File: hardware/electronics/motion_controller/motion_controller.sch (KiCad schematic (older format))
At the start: 181 parts, among them K1 CONN_3, K10 CONN_3, K11 CONN_3, K12 CONN_3, K13 CONN_3, K14 CONN_3, K15 CONN_3, K2 CONN_3, K3 CONN_3, K4 CONN_3, K5 CONN_3, K6 CONN_3, K7 CONN_3, K8 CONN_3, K9 CONN_3, P1 CONN_2, P10 CONN_4, P11 CONN_4, P12 CONN_4, P13 CONN_2, P14 CONN_2, P15 CONN_2, P16 CONN_2, P17 CONN_2, P18 CONN_2, P19 CONN_2X2, P2 CONN_5X2, P20 CONN_2X2, P21 CONN_2, P22 CONN_2, P23 CONN_2, P24 CONN_2, P25 CONN_2, P26 CONN_2X2, P27 CONN_2, P28 CONN_2, P29 CONN_2, P3 CONN_2X2, P4 CONN_2, P5 CONN_34X2, P6 CONN_4, P7 CONN_4, P8 CONN_4, P9 CONN_4, U1 TEENSY3.1, U10 OP07, U12 OP07, U14 OP07, U16 OP07, U18 OP07, U2 NC7WZ04, U20 OP07, U22 OP07, U24 OP07, U26 OP07, U27 MEA1D0512SC, U3 NC7WZ16, U4 NC7WZ16, U5 SSR_DC_6PIN, U6 MAX6176AASA+, U8 OP07

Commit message: Worked on layout.
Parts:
- renumbered U14 to U10, U16 to U11, U18 to U12, U20 to U13, U22 to U14, U24 to U15, U26 to U16, U27 to U17, U8 to U7, U10 to U8, U12 to U9
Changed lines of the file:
@@
 Stepper/Servo Motors
 $Comp
-L OP07 U8
+L OP07 U7
 U 1 1 56F328BD
 P 13850 1450
-F 0 "U8" H 13850 1800 60  0000 C CNN
+F 0 "U7" H 13850 1800 60  0000 C CNN
 F 1 "OP07" H 13850 1150 60  0000 C CNN
 F 2 "~" H 13880 1450 60  0000 C CNN
@@
 GND
 $Comp
-L OP07 U10
+L OP07 U8
 U 1 1 56F34AA5
 P 13850 2550
-F 0 "U10" H 13850 2900 60  0000 C CNN
+F 0 "U8" H 13850 2900 60  0000 C CNN
 F 1 "OP07" H 13850 2250 60  0000 C CNN
 F 2 "~" H 13880 2550 60  0000 C CNN
@@
 10V_REF
 $Comp
-L OP07 U12
+L OP07 U9
 U 1 1 56F34AE7
 P 13850 3650
-F 0 "U12" H 13850 4000 60  0000 C CNN
+F 0 "U9" H 13850 4000 60  0000 C CNN
 F 1 "OP07" H 13850 3350 60  0000 C CNN
 F 2 "~" H 13880 3650 60  0000 C CNN
@@
 10V_REF
 $Comp
-L OP07 U14
+L OP07 U10
 U 1 1 56F34B29
 P 13850 4750
-F 0 "U14" H 13850 5100 60  0000 C CNN
+F 0 "U10" H 13850 5100 60  0000 C CNN
 F 1 "OP07" H 13850 4450 60  0000 C CNN
 F 2 "~" H 13880 4750 60  0000 C CNN
@@
 10V_REF
 $Comp
-L OP07 U16
+L OP07 U11
 U 1 1 56F34B6B
 P 13850 5800
-F 0 "U16" H 13850 6150 60  0000 C CNN
+F 0 "U11" H 13850 6150 60  0000 C CNN
 F 1 "OP07" H 13850 5500 60  0000 C CNN
 F 2 "~" H 13880 5800 60  0000 C CNN
@@
 10V_REF
 $Comp
-L OP07 U18
+L OP07 U12
 U 1 1 56F34BAD
 P 13850 6900
-F 0 "U18" H 13850 7250 60  0000 C CNN
+F 0 "U12" H 13850 7250 60  0000 C CNN
 F 1 "OP07" H 13850 6600 60  0000 C CNN
 F 2 "~" H 13880 6900 60  0000 C CNN
@@
 10V_REF
 $Comp
-L OP07 U20
+L OP07 U13
 U 1 1 56F34BEF
 P 13850 8000
-F 0 "U20" H 13850 8350 60  0000 C CNN
+F 0 "U13" H 13850 8350 60  0000 C CNN
 F 1 "OP07" H 13850 7700 60  0000 C CNN
 F 2 "~" H 13880 8000 60  0000 C CNN
@@
 10V_REF
 $Comp
-L OP07 U22
+L OP07 U14
 U 1 1 56F34C31
 P 13850 9100
-F 0 "U22" H 13850 9450 60  0000 C CNN
+F 0 "U14" H 13850 9450 60  0000 C CNN
 F 1 "OP07" H 13850 8800 60  0000 C CNN
 F 2 "~" H 13880 9100 60  0000 C CNN
@@
 10V_REF
 $Comp
-L OP07 U24
+L OP07 U15
 U 1 1 56F3576B
 P 13850 10200
-F 0 "U24" H 13850 10550 60  0000 C CNN
+F 0 "U15" H 13850 10550 60  0000 C CNN
 F 1 "OP07" H 13850 9900 60  0000 C CNN
 F 2 "~" H 13880 10200 60  0000 C CNN
@@
 DIR1_SEL
 $Comp
-L MEA1D0512SC U27
+L MEA1D0512SC U17
 U 1 1 56F372AA
 P 10050 12900
-F 0 "U27" H 10050 13350 60  0000 C CNN
+F 0 "U17" H 10050 13350 60  0000 C CNN
 F 1 "MEA1D0512SC" H 10050 12450 60  0000 C CNN
 F 2 "~" H 9950 12800 60  0000 C CNN
@@
 -12V
 $Comp
-L OP07 U26
+L OP07 U16
 U 1 1 56F3B380
 P 13850 11300
-F 0 "U26" H 13850 11650 60  0000 C CNN
+F 0 "U16" H 13850 11650 60  0000 C CNN
 F 1 "OP07" H 13850 11000 60  0000 C CNN
 F 2 "~" H 13880 11300 60  0000 C CNN

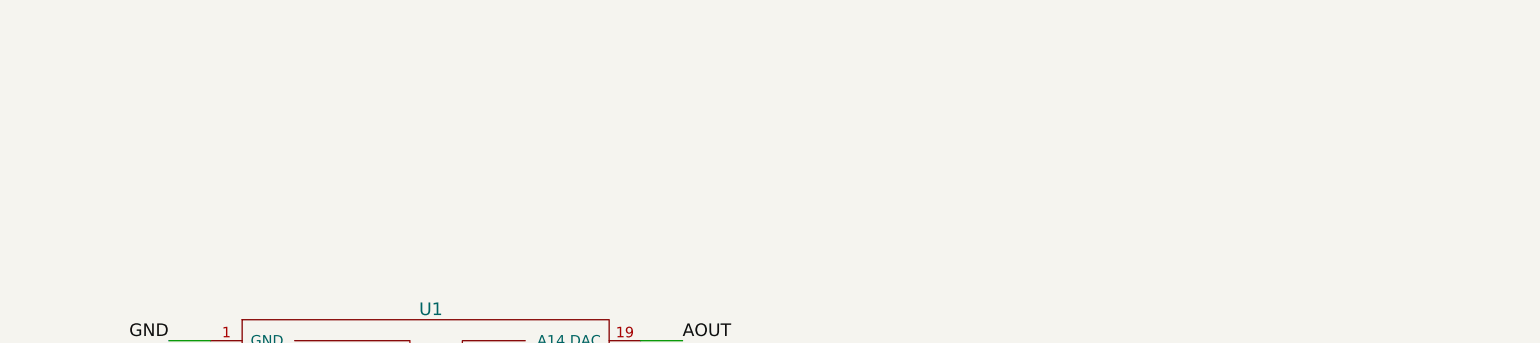
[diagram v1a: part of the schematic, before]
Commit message: Worked on motion controller PCB layout.
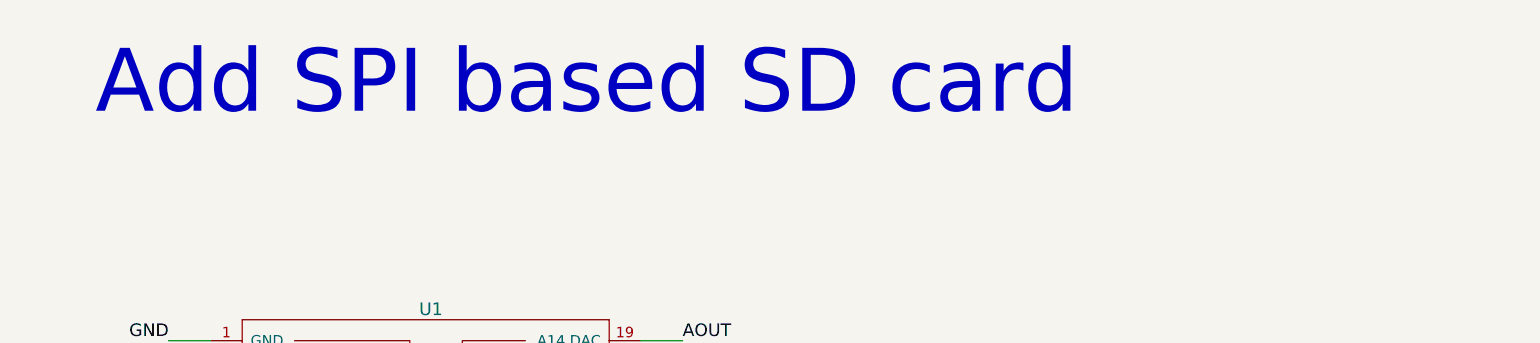
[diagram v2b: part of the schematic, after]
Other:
- note added: "Add SPI based SD card"
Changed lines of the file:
@@
 Sheet 1 1
 Title ""
-Date "5 apr 2016"
+Date "7 apr 2016"
 Rev ""
 Comp ""
@@
 Text Notes 15450 850  0    60   ~ 0
 BAS70-04-E3-08
+Text Notes 750  -150 0    300  ~ 0
+Add SPI based SD card
 $EndSCHEMATC

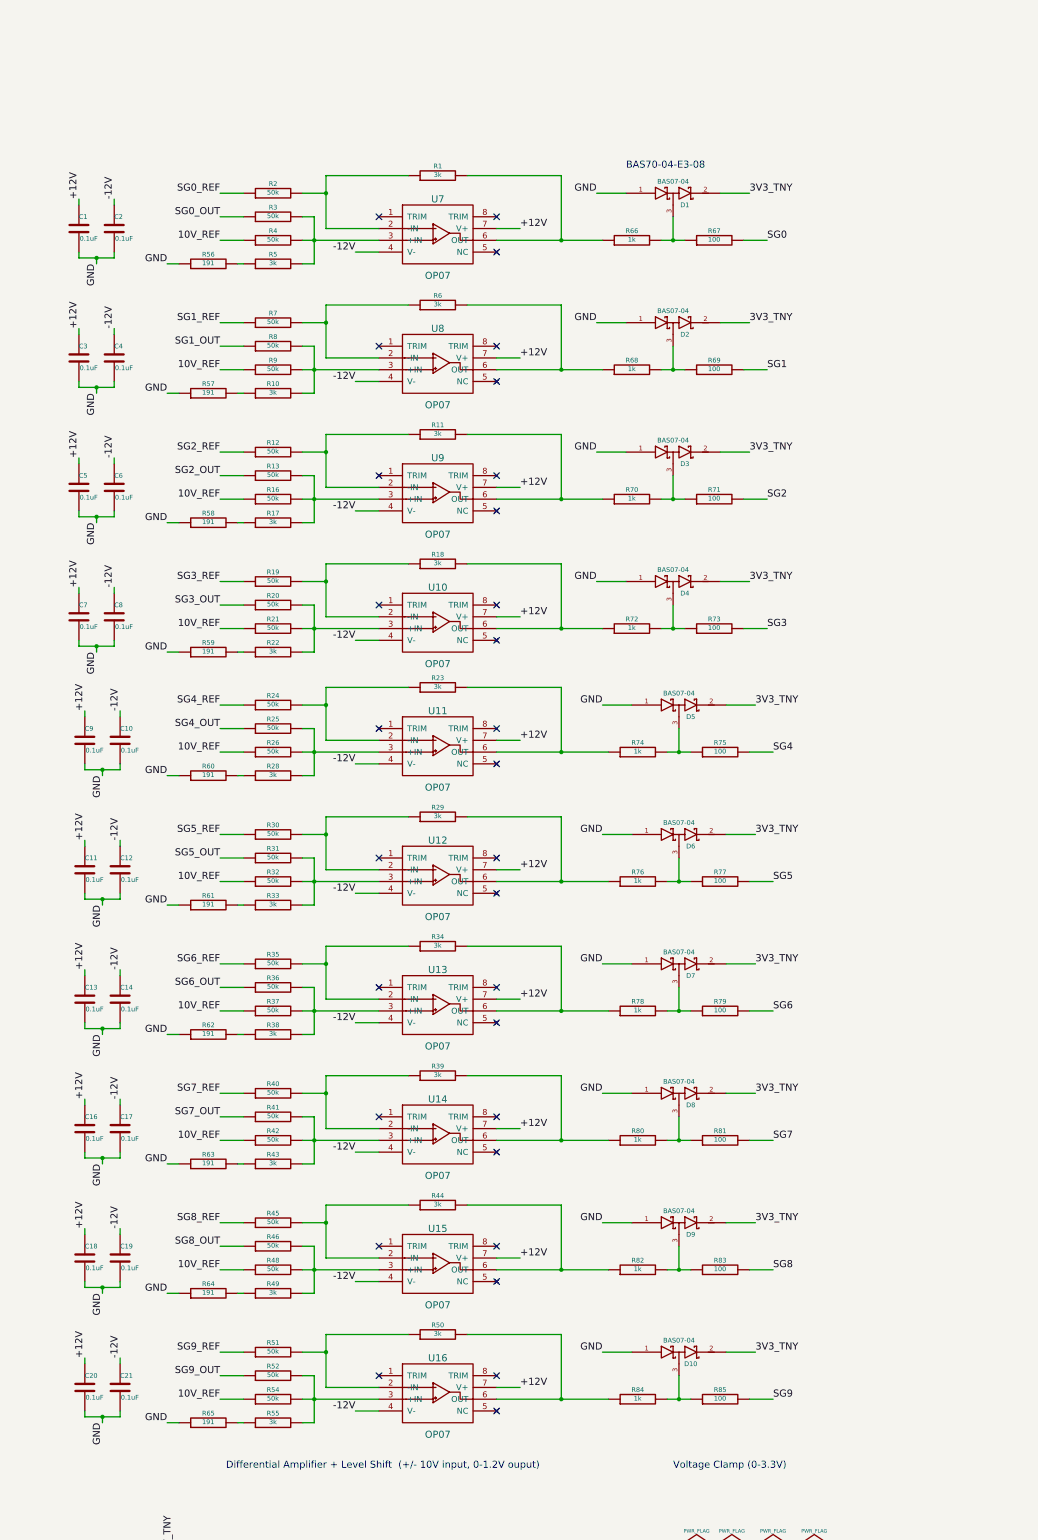
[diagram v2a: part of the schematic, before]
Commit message: Worked on layout of analog input subsystem.
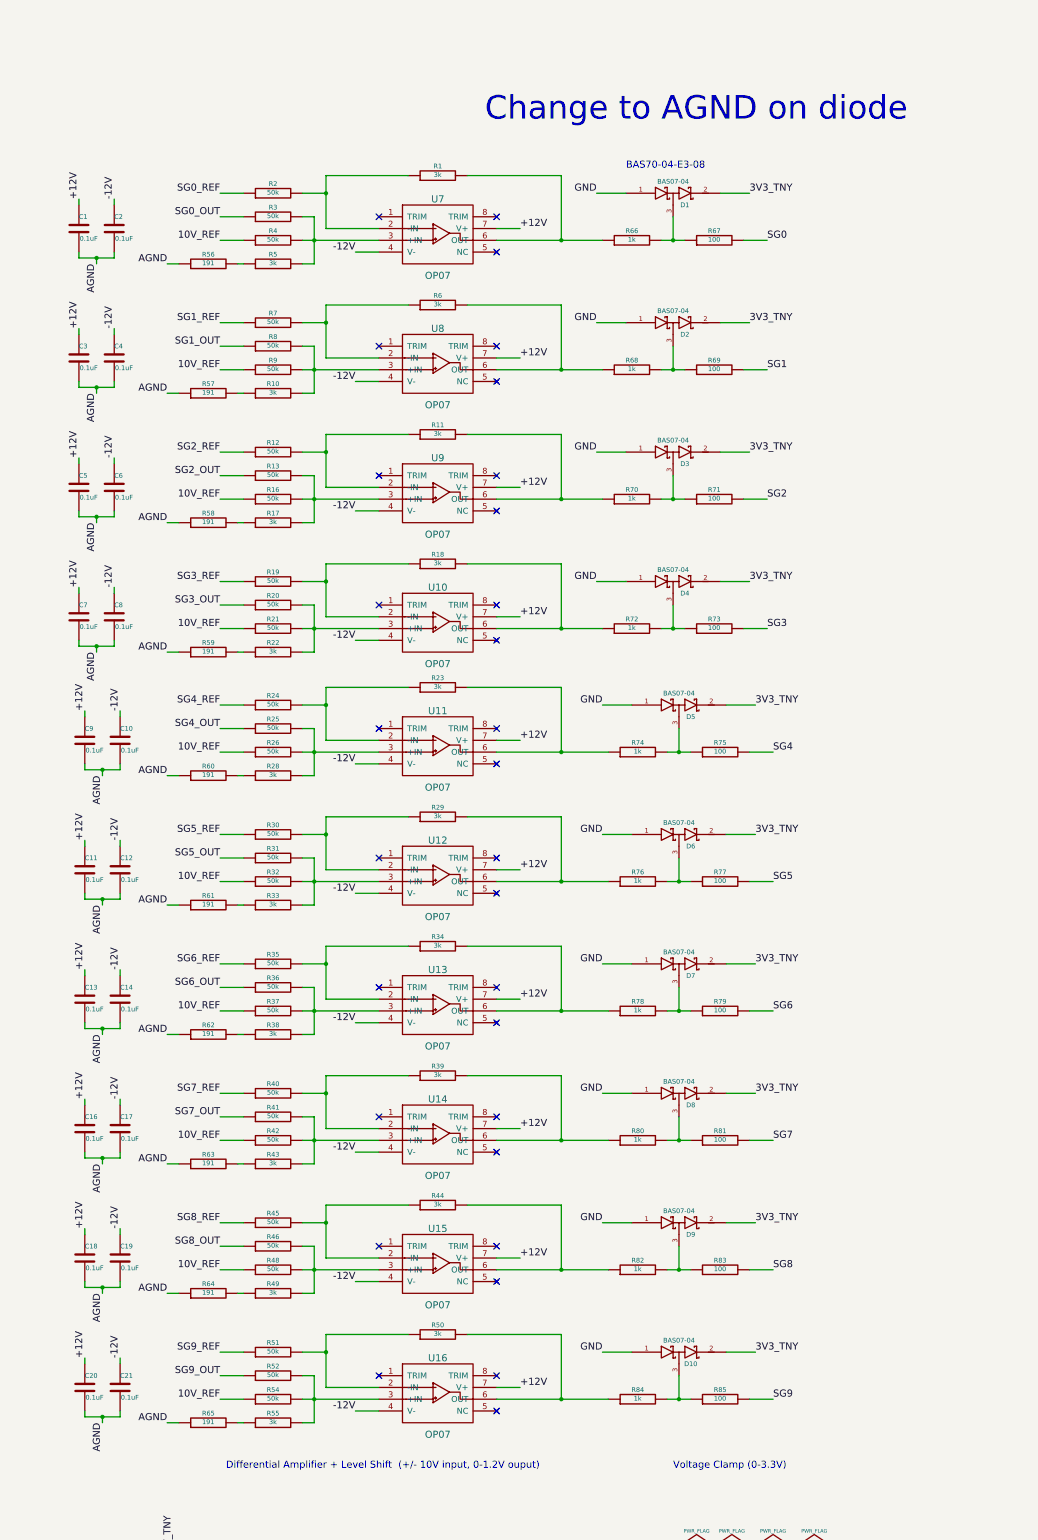
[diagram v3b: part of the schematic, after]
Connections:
- net AGND: now also C1.2, C10.2, C11.2, C12.2, C13.2, C14.2, C16.2, C17.2, C18.2, C19.2, C2.2, C20.2, C21.2, C3.2, C4.2, C5.2, C6.2, C7.2, C8.2, C9.2, R56.1, R57.1, R58.1, R59.1, R60.1, R61.1, R62.1, R63.1, R64.1, R65.1
- net GND: no longer C1.2, C10.2, C11.2, C12.2, C13.2, C14.2, C16.2, C17.2, C18.2, C19.2, C2.2, C20.2, C21.2, C3.2, C4.2, C5.2, C6.2, C7.2, C8.2, C9.2, R56.1, R57.1, R58.1, R59.1, R60.1, R61.1, R62.1, R63.1, R64.1, R65.1
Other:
- note added: "Change to AGND on diode"
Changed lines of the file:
@@
 Sheet 1 1
 Title ""
-Date "7 apr 2016"
+Date "8 apr 2016"
 Rev ""
 Comp ""
@@
 10V_REF
 Text Label 11550 1650 2    60   ~ 0
-GND
+AGND
 $Comp
 L OP07 U8
@@
 $EndComp
 Text Label 10950 1650 3    60   ~ 0
-GND
+AGND
 Text Label 10800 1100 1    60   ~ 0
 +12V
@@
 $EndComp
 Text Label 10950 2750 3    60   ~ 0
-GND
+AGND
 Text Label 10800 2200 1    60   ~ 0
 +12V
@@
 $EndComp
 Text Label 10950 3850 3    60   ~ 0
-GND
+AGND
 Text Label 10800 3300 1    60   ~ 0
 +12V
@@
 $EndComp
 Text Label 10950 4950 3    60   ~ 0
-GND
+AGND
 Text Label 10800 4400 1    60   ~ 0
 +12V
@@
 $EndComp
 Text Label 11000 6000 3    60   ~ 0
-GND
+AGND
 Text Label 10850 5450 1    60   ~ 0
 +12V
@@
 $EndComp
 Text Label 11000 7100 3    60   ~ 0
-GND
+AGND
 Text Label 10850 6550 1    60   ~ 0
 +12V
@@
 $EndComp
 Text Label 11000 8200 3    60   ~ 0
-GND
+AGND
 Text Label 10850 7650 1    60   ~ 0
 +12V
@@
 $EndComp
 Text Label 11000 9300 3    60   ~ 0
-GND
+AGND
 Text Label 10850 8750 1    60   ~ 0
 +12V
@@
 $EndComp
 Text Label 11000 10400 3    60   ~ 0
-GND
+AGND
 Text Label 10850 9850 1    60   ~ 0
 +12V
@@
 $EndComp
 Text Label 11000 11500 3    60   ~ 0
-GND
+AGND
 Text Label 10850 10950 1    60   ~ 0
 +12V
@@
 $EndComp
 Text Label 11550 2750 2    60   ~ 0
-GND
+AGND
 $Comp
 L R R57
@@
 $EndComp
 Text Label 11550 3850 2    60   ~ 0
-GND
+AGND
 $Comp
 L R R58
@@
 $EndComp
 Text Label 11550 4950 2    60   ~ 0
-GND
+AGND
 $Comp
 L R R59
@@
 $EndComp
 Text Label 11550 6000 2    60   ~ 0
-GND
+AGND
 $Comp
 L R R60
@@
 $EndComp
 Text Label 11550 7100 2    60   ~ 0
-GND
+AGND
 $Comp
 L R R61
@@
 $EndComp
 Text Label 11550 8200 2    60   ~ 0
-GND
+AGND
 $Comp
 L R R62
@@
 $EndComp
 Text Label 11550 9300 2    60   ~ 0
-GND
+AGND
 $Comp
 L R R63
@@
 $EndComp
 Text Label 11550 10400 2    60   ~ 0
-GND
+AGND
 $Comp
 L R R64
@@
 $EndComp
 Text Label 11550 11500 2    60   ~ 0
-GND
+AGND
 $Comp
 L R R65
@@
 Text Notes 750  -150 0    300  ~ 0
 Add SPI based SD card
+Text Notes 14250 450  0    200  ~ 0
+Change to AGND on diode
 $EndSCHEMATC

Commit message: Added PJRC SD card. Changed so that double schottky diodes in a analog clamp use AGND instead of GND. Worked on layout.
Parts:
- added U18: PJRC_SD_CARD, ~, symbol PJRC_SD_CARD
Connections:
- net 5V_TNY: now also U18.10 (5V)
- net AGND: now also D1.1 (Anode), D10.1 (Anode), D2.1 (Anode), D3.1 (Anode), D4.1 (Anode), D5.1 (Anode), D6.1 (Anode), D7.1 (Anode), D8.1 (Anode), D9.1 (Anode)
- net D11,MOSI: now also U18.4 (MOSI)
- net D12,MISO: now also U18.5 (MISO)
- net D13,SCK: now also U18.3 (SCLK)
- net GND: now also U18.1 (GND); no longer D1.1 (Anode), D10.1 (Anode), D2.1 (Anode), D3.1 (Anode), D4.1 (Anode), D5.1 (Anode), D6.1 (Anode), D7.1 (Anode), D8.1 (Anode), D9.1 (Anode)
- net PWM4,D10,CS: now also U18.2 (SS)
- no-connect marks 88 -> 92
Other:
- note removed: "Add SPI based SD card"
- moved on the sheet: P1
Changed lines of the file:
@@
 LIBS:max4505
 LIBS:bas07-04
+LIBS:pjrc_sd_card
 LIBS:motion_controller-cache
 EELAYER 27 0
@@
 L CONN_2 P1
 U 1 1 56F4265C
-P 8900 1150
-F 0 "P1" V 8850 1150 40  0000 C CNN
-F 1 "CONN_2" V 8950 1150 40  0000 C CNN
-F 2 "" H 8900 1150 60  0000 C CNN
-F 3 "" H 8900 1150 60  0000 C CNN
-	1    8900 1150
+P 4000 7450
+F 0 "P1" V 3950 7450 40  0000 C CNN
+F 1 "CONN_2" V 4050 7450 40  0000 C CNN
+F 2 "" H 4000 7450 60  0000 C CNN
+F 3 "" H 4000 7450 60  0000 C CNN
+	1    4000 7450
 	1    0    0    -1
 $EndComp
-Text Label 8300 1050 2    60   ~ 0
+Text Label 3400 7350 2    60   ~ 0
 AOUT
-Text Label 8300 1250 2    60   ~ 0
+Text Label 3400 7550 2    60   ~ 0
 GND
-Text Notes 8100 1550 0    60   ~ 0
+Text Notes 3200 7850 0    60   ~ 0
 Analog Output (0-3.3V)
 $Comp
@@
 3V3_TNY
 Text Label 15200 1050 2    60   ~ 0
-GND
+AGND
 Text Label 16650 1450 0    60   ~ 0
 SG0
@@
 	11600 13200 11600 13400
 Wire Wire Line
-	8550 1050 8300 1050
+	3650 7350 3400 7350
 Wire Wire Line
-	8550 1250 8300 1250
+	3650 7550 3400 7550
 Wire Wire Line
 	3600 6550 3400 6550
@@
 3V3_TNY
 Text Label 15200 2150 2    60   ~ 0
-GND
+AGND
 Text Label 16650 2550 0    60   ~ 0
 SG1
@@
 3V3_TNY
 Text Label 15200 3250 2    60   ~ 0
-GND
+AGND
 Text Label 16650 3650 0    60   ~ 0
 SG2
@@
 3V3_TNY
 Text Label 15200 4350 2    60   ~ 0
-GND
+AGND
 Text Label 16650 4750 0    60   ~ 0
 SG3
@@
 3V3_TNY
 Text Label 15250 5400 2    60   ~ 0
-GND
+AGND
 Text Label 16700 5800 0    60   ~ 0
 SG4
@@
 3V3_TNY
 Text Label 15250 6500 2    60   ~ 0
-GND
+AGND
 Text Label 16700 6900 0    60   ~ 0
 SG5
@@
 3V3_TNY
 Text Label 15250 7600 2    60   ~ 0
-GND
+AGND
 Text Label 16700 8000 0    60   ~ 0
 SG6
@@
 3V3_TNY
 Text Label 15250 8700 2    60   ~ 0
-GND
+AGND
 Text Label 16700 9100 0    60   ~ 0
 SG7
@@
 3V3_TNY
 Text Label 15250 9800 2    60   ~ 0
-GND
+AGND
 Text Label 16700 10200 0    60   ~ 0
 SG8
@@
 3V3_TNY
 Text Label 15250 10900 2    60   ~ 0
-GND
+AGND
 Text Label 16700 11300 0    60   ~ 0
 SG9
@@
 Text Notes 15450 850  0    60   ~ 0
 BAS70-04-E3-08
-Text Notes 750  -150 0    300  ~ 0
-Add SPI based SD card
 Text Notes 14250 450  0    200  ~ 0
 Change to AGND on diode
+$Comp
+L PJRC_SD_CARD U18
+U 1 1 57081353
+P 8600 1250
+F 0 "U18" H 8600 1600 60  0000 C CNN
+F 1 "PJRC_SD_CARD" H 8600 900 60  0000 C CNN
+F 2 "~" H 8850 1150 60  0000 C CNN
+F 3 "~" H 8850 1150 60  0000 C CNN
+	1    8600 1250
+	1    0    0    -1
+$EndComp
+Wire Wire Line
+	8000 1050 7800 1050
+Wire Wire Line
+	8000 1150 7800 1150
+Wire Wire Line
+	8000 1250 7800 1250
+Wire Wire Line
+	8000 1350 7800 1350
+Wire Wire Line
+	8000 1450 7800 1450
+Wire Wire Line
+	9200 1050 9400 1050
+NoConn ~ 9200 1150
+NoConn ~ 9200 1250
+NoConn ~ 9200 1350
+NoConn ~ 9200 1450
+Text Label 7800 1050 2    60   ~ 0
+GND
+Text Label 7800 1250 2    60   ~ 0
+D13,SCK
+Text Label 7800 1150 2    60   ~ 0
+PWM4,D10,CS
+Text Label 7800 1350 2    60   ~ 0
+D11,MOSI
+Text Label 7800 1450 2    60   ~ 0
+D12,MISO
+Text Label 9400 1050 0    60   ~ 0
+5V_TNY
 $EndSCHEMATC

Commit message: Finished initial layout of motion controller pcb.
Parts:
- added P30, P31, P32, P33: CONN_1, symbol CONN_1
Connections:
- net GND: now also P30.1, P31.1, P32.1, P33.1
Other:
- note added: "Mount Holes"
- note removed: "Change to AGND on diode"
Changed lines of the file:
@@
 Sheet 1 1
 Title ""
-Date "8 apr 2016"
+Date "9 apr 2016"
 Rev ""
 Comp ""
@@
 Text Notes 15450 850  0    60   ~ 0
 BAS70-04-E3-08
-Text Notes 14250 450  0    200  ~ 0
-Change to AGND on diode
 $Comp
 L PJRC_SD_CARD U18
@@
 Text Label 9400 1050 0    60   ~ 0
 5V_TNY
+$Comp
+L CONN_1 P30
+U 1 1 57085C98
+P 12800 13350
+F 0 "P30" H 12880 13350 40  0000 L CNN
+F 1 "CONN_1" H 12800 13405 30  0001 C CNN
+F 2 "" H 12800 13350 60  0000 C CNN
+F 3 "" H 12800 13350 60  0000 C CNN
+	1    12800 13350
+	1    0    0    -1
+$EndComp
+$Comp
+L CONN_1 P31
+U 1 1 57085CA7
+P 12800 13450
+F 0 "P31" H 12880 13450 40  0000 L CNN
+F 1 "CONN_1" H 12800 13505 30  0001 C CNN
+F 2 "" H 12800 13450 60  0000 C CNN
+F 3 "" H 12800 13450 60  0000 C CNN
+	1    12800 13450
+	1    0    0    -1
+$EndComp
+$Comp
+L CONN_1 P32
+U 1 1 57085CB6
+P 12800 13550
+F 0 "P32" H 12880 13550 40  0000 L CNN
+F 1 "CONN_1" H 12800 13605 30  0001 C CNN
+F 2 "" H 12800 13550 60  0000 C CNN
+F 3 "" H 12800 13550 60  0000 C CNN
+	1    12800 13550
+	1    0    0    -1
+$EndComp
+$Comp
+L CONN_1 P33
+U 1 1 57085CC5
+P 12800 13650
+F 0 "P33" H 12880 13650 40  0000 L CNN
+F 1 "CONN_1" H 12800 13705 30  0001 C CNN
+F 2 "" H 12800 13650 60  0000 C CNN
+F 3 "" H 12800 13650 60  0000 C CNN
+	1    12800 13650
+	1    0    0    -1
+$EndComp
+Wire Wire Line
+	12650 13350 12550 13350
+Wire Wire Line
+	12550 13350 12550 13650
+Wire Wire Line
+	12350 13650 12650 13650
+Wire Wire Line
+	12650 13450 12550 13450
+Connection ~ 12550 13450
+Wire Wire Line
+	12650 13550 12550 13550
+Connection ~ 12550 13550
+Connection ~ 12550 13650
+Text Label 12350 13650 2    60   ~ 0
+GND
+Text Notes 12300 13800 0    60   ~ 0
+Mount Holes
 $EndSCHEMATC
